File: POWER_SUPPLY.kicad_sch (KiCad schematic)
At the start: 4 parts, among them J1 Jack-DC, J2 USB_B_Micro, U4 LMR33640ADDA, U5 LMR33640ADDA

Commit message: Weiter gearbeitet
Fast fertig:
HUB
Fertig
Connector (Up and Down)
MUX
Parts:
- added C85, C86, C87: 10u, Capacitor_SMD:C_0603_1608Metric, symbol Device:C
- added R53, R54, R55, R56, R57, R58: R, symbol Device:R
- added U19, U20: LM66100DCK, Package_TO_SOT_SMD:SOT-363_SC-70-6, symbol Power_Management:LM66100DCK
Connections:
- net at J2.1 (VBUS): now also C87.1, R56.1, U20.1 (VIN)
- net GND: now reaches J2.5 (GND)
- net GND: now also J1.2, J2.6 (Shield), C85.2, C86.2, C87.2, R54.2, R57.2, U19.2 (GND), U20.2 (GND)
- net at J1.1: now also C85.1, R53.1, U19.1 (VIN)
- new net: R55.2, U19.5 (ST)
- new net: R53.2, R54.1, U19.3 (~{CE})
- new net: R56.2, R57.1, U20.3 (~{CE})
- new net: R58.2, U20.5 (ST)
- new net +5V: C86.1, R55.1, R58.1, U19.6 (VOUT), U20.6 (VOUT)
- no-connect marks 0 -> 3
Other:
- moved on the sheet: J1, J2, U4, U5

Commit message: Footprints Updated
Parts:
- C85, C86, C87: footprint Capacitor_SMD:C_0603_1608Metric -> 00_Capacitor:Cap_0603
- R53, R54, R55, R56, R57, R58: footprint (none) -> 00_Resistor:Res_0402
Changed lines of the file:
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@@
 			)
 		)
-		(property "Footprint" ""
+		(property "Footprint" "00_Resistor:Res_0402"
 			(at 98.552 30.48 90)
 			(effects
@@
 			)
 		)
-		(property "Footprint" ""
+		(property "Footprint" "00_Resistor:Res_0402"
 			(at 62.992 39.37 90)
 			(effects
@@
 			)
 		)
-		(property "Footprint" "Capacitor_SMD:C_0603_1608Metric"
+		(property "Footprint" "00_Capacitor:Cap_0603"
 			(at 130.5052 39.37 0)
 			(effects
@@
 			)
 		)
-		(property "Footprint" "Capacitor_SMD:C_0603_1608Metric"
+		(property "Footprint" "00_Capacitor:Cap_0603"
 			(at 53.0352 34.29 0)
 			(effects
@@
 			)
 		)
-		(property "Footprint" ""
+		(property "Footprint" "00_Resistor:Res_0402"
 			(at 62.992 64.77 90)
 			(effects
@@
 			)
 		)
-		(property "Footprint" ""
+		(property "Footprint" "00_Resistor:Res_0402"
 			(at 62.992 29.21 90)
 			(effects
@@
 			)
 		)
-		(property "Footprint" "Capacitor_SMD:C_0603_1608Metric"
+		(property "Footprint" "00_Capacitor:Cap_0603"
 			(at 53.0352 69.85 0)
 			(effects
@@
 			)
 		)
-		(property "Footprint" ""
+		(property "Footprint" "00_Resistor:Res_0402"
 			(at 98.552 66.04 90)
 			(effects
@@
 			)
 		)
-		(property "Footprint" ""
+		(property "Footprint" "00_Resistor:Res_0402"
 			(at 62.992 74.93 90)
 			(effects

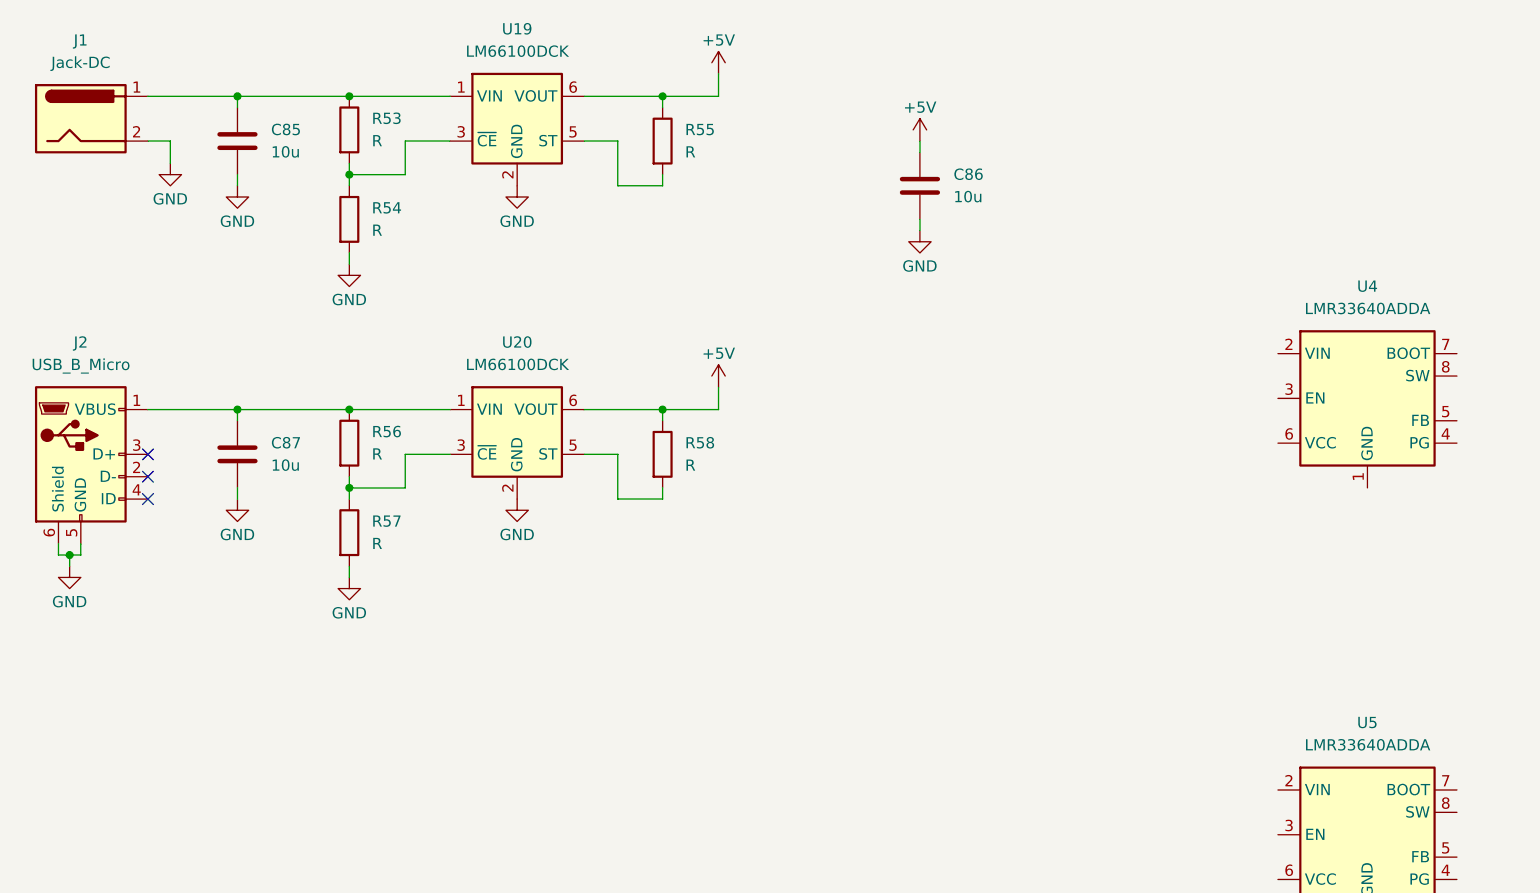
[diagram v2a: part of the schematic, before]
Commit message: USB 3 Stecker ausgetauscht
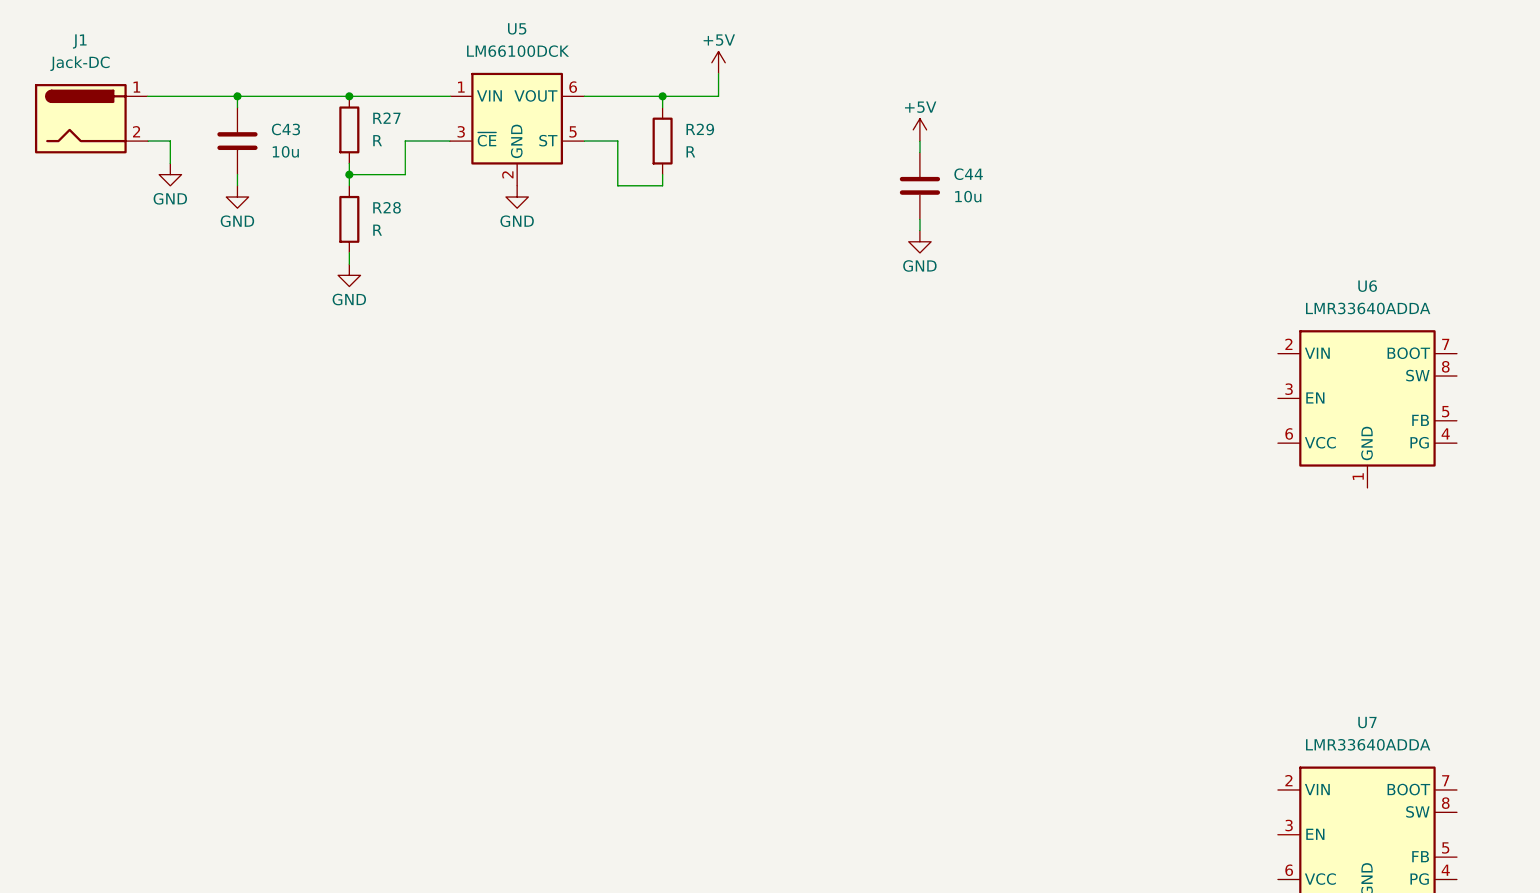
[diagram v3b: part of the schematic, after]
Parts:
- removed C87: 10u, 00_Capacitor:Cap_0603, symbol Device:C
- removed J2: USB_B_Micro, symbol Connector:USB_B_Micro
- removed R56, R57, R58: R, 00_Resistor:Res_0402, symbol Device:R
- removed U20: LM66100DCK, Package_TO_SOT_SMD:SOT-363_SC-70-6, symbol Power_Management:LM66100DCK
- renumbered C85 to C43, C86 to C44, R53 to R27, R54 to R28, R55 to R29, U19 to U5, U4 to U6, U5 to U7
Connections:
- no-connect marks 3 -> 0

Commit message: Weiter gemacht
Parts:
- added C100, C95: 220n, 00_Capacitor:Cap_0402, symbol Device:C
- added C101, C98: 1u, 00_Capacitor:Cap_0402, symbol Device:C_Small
- added C102, C91: 100n, 00_Capacitor:Cap_0402, symbol Device:C_Small
- added C103, C104, C105, C89, C92, C93: 22u, 00_Capacitor:Cap_0805, symbol Device:C
- added C87, C88, C94, C99: 10u, 00_Capacitor:Cap_0603, symbol Device:C
- added C90: 100uF, Capacitor_SMD:CP_Elec_6.3x5.9, symbol Device:C_Polarized
- added L1: 6.8u, Inductor_SMD:L_Coilcraft_XAL7030-272, symbol Device:L
- added L2: 10u, Inductor_SMD:L_Coilcraft_XAL7030-272, symbol Device:L
- added R56, R58: 100k, 00_Capacitor:Cap_0402, symbol Device:R
- added R57: 4.32k, 00_Capacitor:Cap_0402, symbol Device:R
- added R59: 1K, 00_Capacitor:Cap_0402, symbol Device:R
- J1: footprint (none) -> Connector_BarrelJack:BarrelJack_GCT_DCJ200-10-A_Horizontal
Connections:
- net +1V1: now also C103.1, C104.1, C105.1, L2.2, R58.1
- net +3.3V: now also C89.1, C92.1, C93.1, L1.2, R56.1
- net +5V: now also U6.2 (VIN), U7.2 (VIN), C100.1, C87.1, C88.1, C90.1, C94.1, C95.1, C99.1
- net GND: now also U6.1 (GND), U6.9 (GND), U7.1 (GND), U7.9 (GND), C100.2, C101.1, C103.2, C104.2, C105.2, C87.2, C88.2, C89.2, C90.2, C92.2, C93.2, C94.2, C95.2, C98.1, C99.2, R57.2, R59.2
- net BUCK_1V1_EN: now reaches U7.3 (EN)
- net BUCK_1V1_PG: now reaches U7.4 (PG)
- net BUCK_1V1_FB: now reaches U7.5 (FB)
- net BUCK_1V1_FB: now also R58.2, R59.1
- net BUCK_1V1_VCC: now reaches U7.6 (VCC)
- net BUCK_1V1_VCC: now also C101.2
- net at U7.7 (BOOT): now also C102.1
- net LX_1V1: now reaches U7.8 (SW)
- net LX_1V1: now also C102.2, L2.1
- net BUCK_3V3_EN: now reaches U6.3 (EN)
- net BUCK_3V3_PG: now reaches U6.4 (PG)
- net BUCK_3V3_FB: now reaches U6.5 (FB)
- net BUCK_3V3_FB: now also R56.2, R57.1
- net BUCK_3V3_VCC: now reaches U6.6 (VCC)
- net BUCK_3V3_VCC: now also C98.2
- net at U6.7 (BOOT): now also C91.1
- net LX_3V3: now reaches U6.8 (SW)
- net LX_3V3: now also C91.2, L1.1
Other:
- note added: "Coilcraft XAL7030-103ME"
- note added: "Coilcraft XAL7030-682ME"
- moved on the sheet: C43, C44, U6, U7

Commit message: Layout + Schematic weiter gemacht
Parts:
- removed R28: R, 00_Resistor:Res_0402, symbol Device:R
- added C106, C107, C109: 100uF, Capacitor_SMD:CP_Elec_6.3x5.9, symbol Device:C_Polarized
- added C110: 10u, 00_Capacitor:Cap_0603, symbol Device:C
- added C111, C112, C113, C114: 100n, 00_Capacitor:Cap_0402, symbol Device:C
- added D4, D5: BAT54J, Diode_SMD:D_SOD-323F, symbol Diode:BAT54J
- added D6: MM3Z2V4, Diode_SMD:D_SOD-323F, symbol Diode:MM3Zxx
- added Q1, Q2: NTJD4401NT1G, Package_TO_SOT_SMD:SOT-363_SC-70-6, symbol ANR_Blastec_Lib:NTJD4401NT1G
- added R60, R61, R62, R64, R68, R69, R70: 10k, 00_Resistor:Res_0402, symbol Device:R
- added R63, R65, R66: 100, 00_Resistor:Res_0402, symbol Device:R
- added R67: 1M, 00_Resistor:Res_0402, symbol Device:R
- added U20, U21: 74LVC1G08, Package_TO_SOT_SMD:SOT-23-5, symbol 74xGxx:74LVC1G08
- added U22: LM397, Package_TO_SOT_SMD:SOT-23-5, symbol Comparator:LM397
- L1, L2: footprint Inductor_SMD:L_Coilcraft_XAL7030-272 -> Inductor_SMD:L_Wuerth_MAPI-3020
- R27: value R -> 1k
- R29: value R -> 10k
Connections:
- net +1V1: now also R66.1
- net +3.3V: now also C112.1, C113.1, C114.1, R60.1, R61.1, R62.1, R65.1, U20.5 (VCC), U21.5 (VCC)
- net +5V: now also R27.1, C106.1, C107.1, C109.1, D5.2 (A), R63.1
- net BUCK_1V1_PG: now also R61.2, U20.2
- net BUCK_3V3_PG: now also R60.2, U21.2
- net GND: now also C106.2, C107.2, C109.2, C110.2, C111.2, C112.2, C113.2, C114.2, D6.2 (A), Q1.1 (S), Q1.4 (S), Q2.1 (S), Q2.4 (S), R67.2, R69.2, U20.3 (GND), U21.3 (GND), U22.2 (V-)
- net ~{RESET}: now also U20.4
- net U5_ST: now reaches R29.2, U5.5 (ST)
- net VIN: now reaches C43.1, J1.1, U5.1 (VIN)
- net VIN: now also C111.1, R68.1, R70.2, U22.5 (V+); no longer R27.1
- new net: C110.1, D5.1 (K), R64.1
- new net: Q1.5 (G), Q1.6 (D), Q2.2 (G), Q2.5 (G), R64.2, R67.1
- new net: Q2.3 (D), R65.2
- new net: D4.2 (A), R62.2, U21.1
- new net: U20.1, U21.4
- new net: Q1.3 (D), R63.2
- new net: Q2.6 (D), R66.2
- new net: R68.2, R69.1, U22.3 (+)
- new net VIN_PGOOD: D4.1 (K), Q1.2 (G), U22.4
- new net VREF: D6.1 (K), R70.1, U22.1 (-)
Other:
- note added: "+1.1V USB HUB core power rail"
- note added: "+3.3V board power"
- note added: "Discharge in case of Power Loss"
- note added: "MAPI3020"
- note removed: "Coilcraft XAL7030-103ME"
- note removed: "Coilcraft XAL7030-682ME"
- moved on the sheet: C100, C101, C102, C103, C104, C105, C43, C89, C91, C92, C93, C94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

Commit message: Power SupV
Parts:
- added Q3: NTJD4401NT1G, Package_TO_SOT_SMD:SOT-363_SC-70-6, symbol ANR_Blastec_Lib:NTJD4401NT1G
- added R71: 1k, 00_Resistor:Res_0402, symbol Device:R
- R64: value 10k -> 1k
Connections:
- net +5V: now also R71.1
- net GND: now also Q3.1 (S)
- net VIN_PGOOD: now also Q3.2 (G); no longer Q1.2 (G)
- new net: Q1.2 (G), Q3.6 (D), R71.2

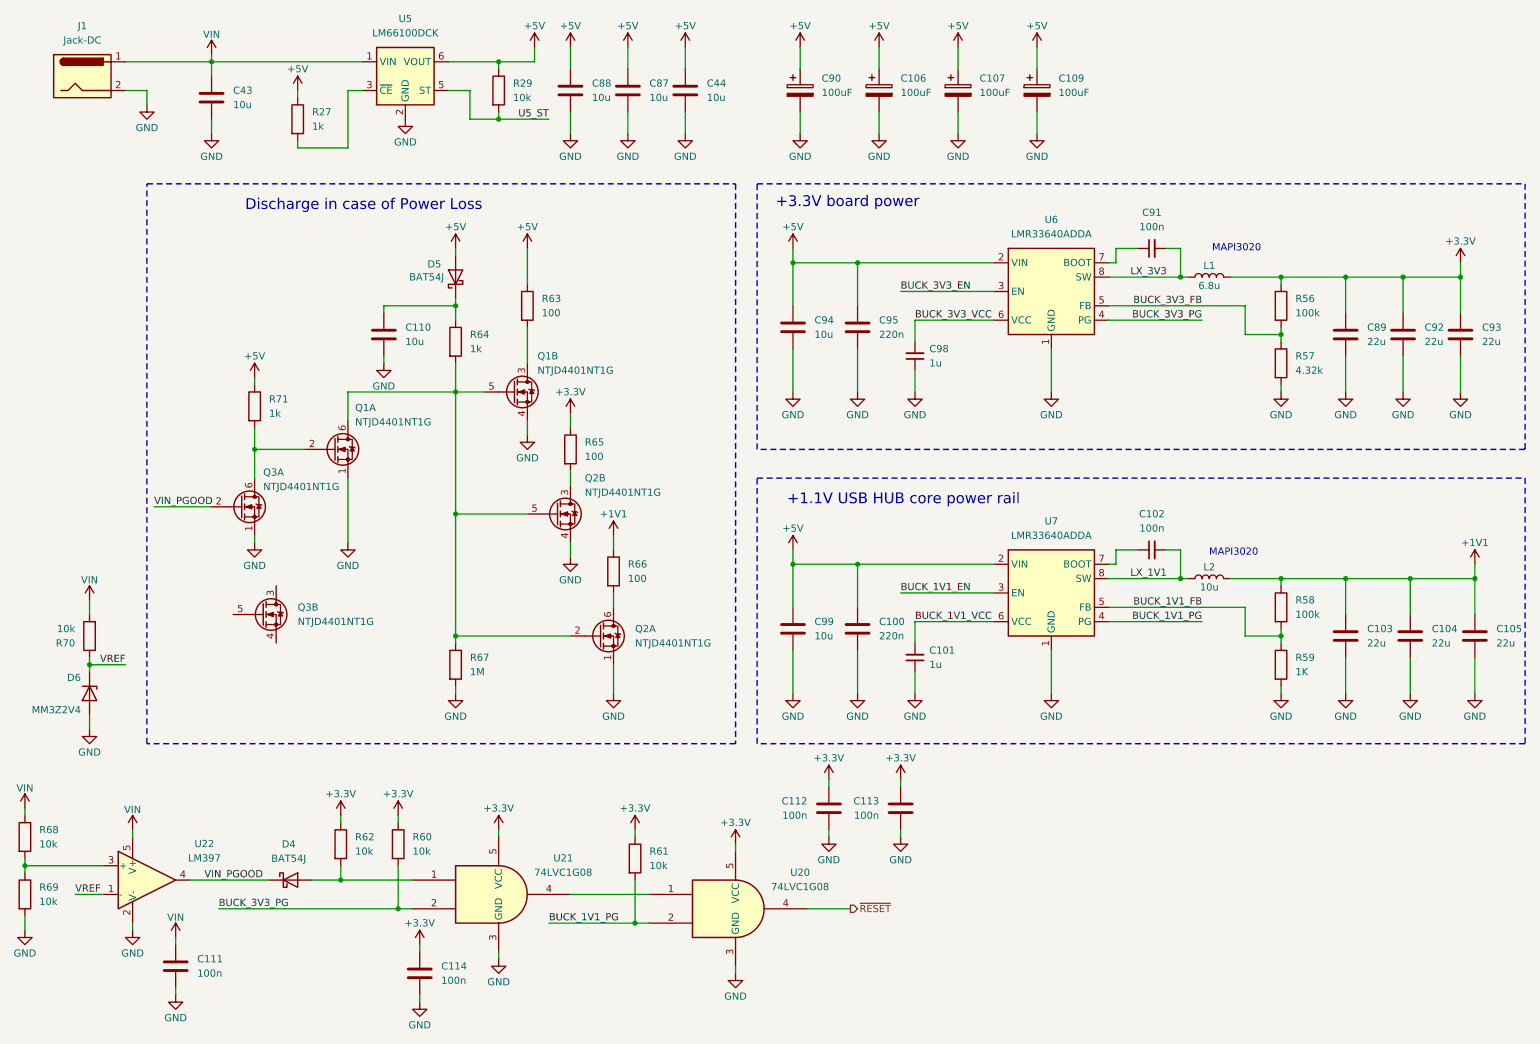
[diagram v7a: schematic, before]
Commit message: Button & Power Sequencing + Layout
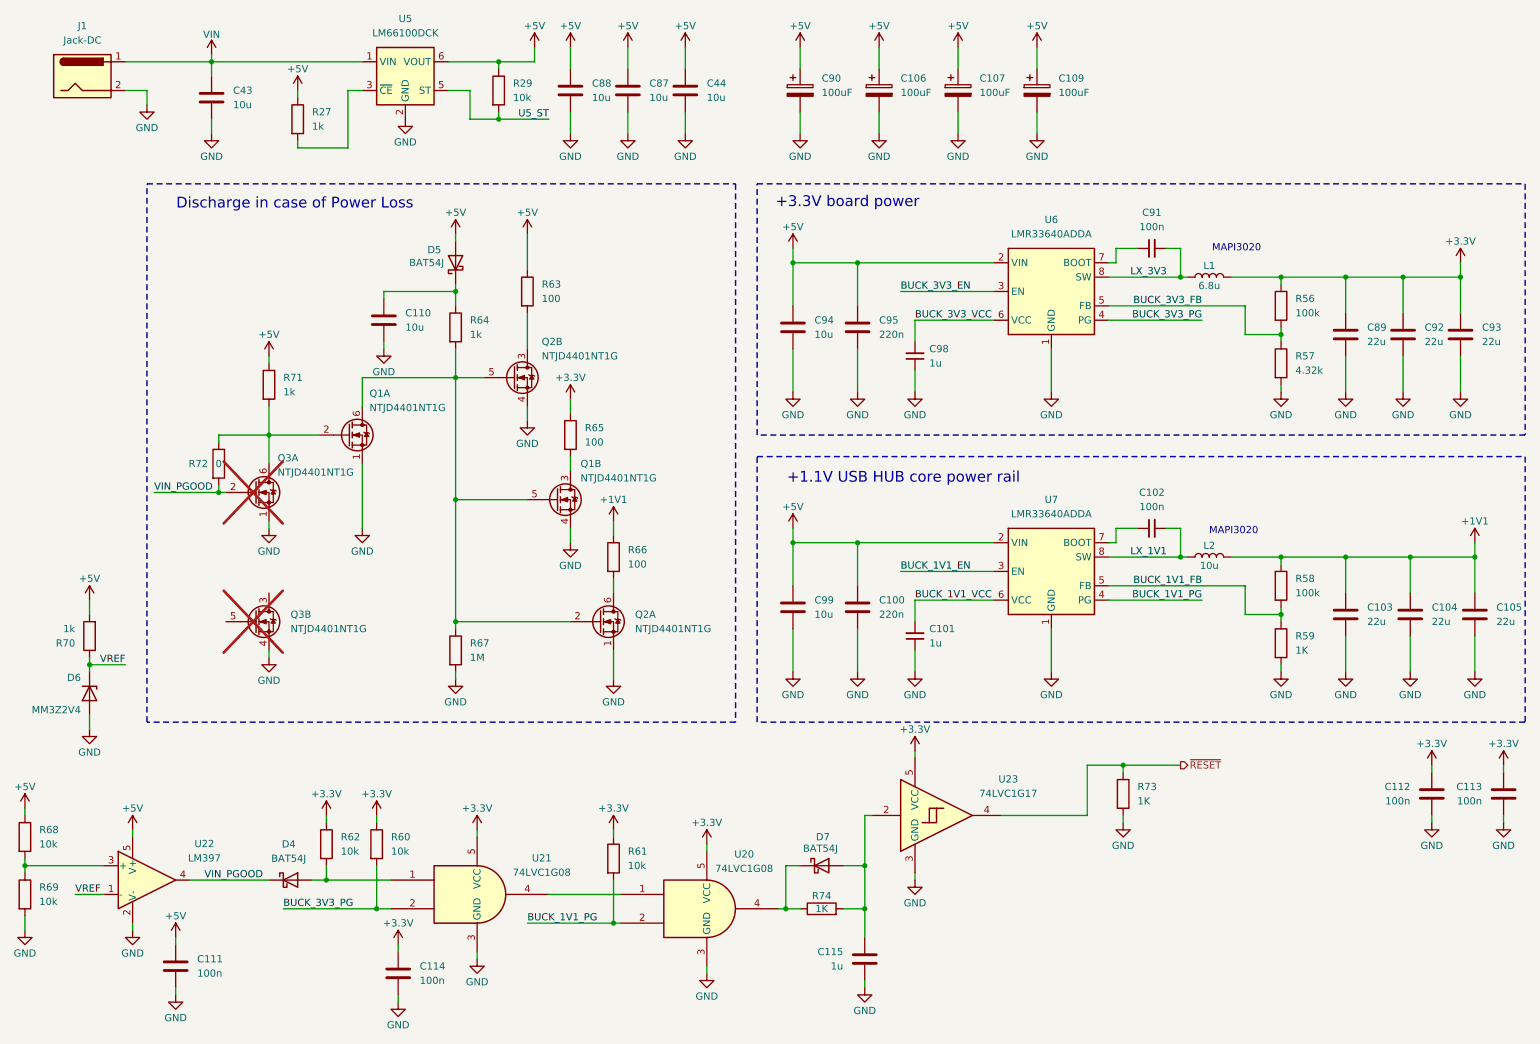
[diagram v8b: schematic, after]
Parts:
- added C115: 1u, 00_Capacitor:Cap_0402, symbol Device:C
- added D7: BAT54J, Diode_SMD:D_SOD-323F, symbol Diode:BAT54J
- added R72: 0, 00_Resistor:Res_0402, symbol Device:R
- added R73, R74: 1K, 00_Capacitor:Cap_0402, symbol Device:R
- added U23: 74LVC1G17, Package_TO_SOT_SMD:SOT-23-5, symbol 74xGxx:74LVC1G17
- Q3: now not fitted
- R70: value 10k -> 1k
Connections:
- net +3.3V: now also U23.5 (VCC)
- net +5V: now also C111.1, R68.1, R70.2, U22.5 (V+)
- net GND: now also Q3.4 (S), C115.2, R73.2, U23.3 (GND)
- net VIN: no longer C111.1, R68.1, R70.2, U22.5 (V+)
- net VIN_PGOOD: now also R72.2
- net ~{RESET}: now also R73.1, U23.4; no longer U20.4
- net at R65.2: now also Q1.3 (D); no longer Q2.3 (D)
- net at R63.2: now also Q2.3 (D); no longer Q1.3 (D)
- net at Q1.2 (G), Q3.6 (D), R71.2: now also R72.1
- new net: D7.1 (K), R74.1, U20.4
- new net: C115.1, D7.2 (A), R74.2, U23.2
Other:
- moved on the sheet: C100, C101, C102, C103, C104, C105, C110, C112, C113, C99, D5, L2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
